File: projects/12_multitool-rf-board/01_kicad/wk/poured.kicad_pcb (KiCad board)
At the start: 4 copper layers, 150 x 150 mm, 87 parts, among them M1 vibro, SW1 RFswitch, SW2 RFswitch, U1 STM32WB55RG, U10 ESD, U2 CC1101, U3 ST25R3916, U5 ST7565R, U6 BQ25896, U7 BQ27220, U8 LM3281, U8B LM3281, U9 loadsw, X10 BAT+NTC, X6 FFC 18p, Y1 32MHz, Y2 32.768kHz

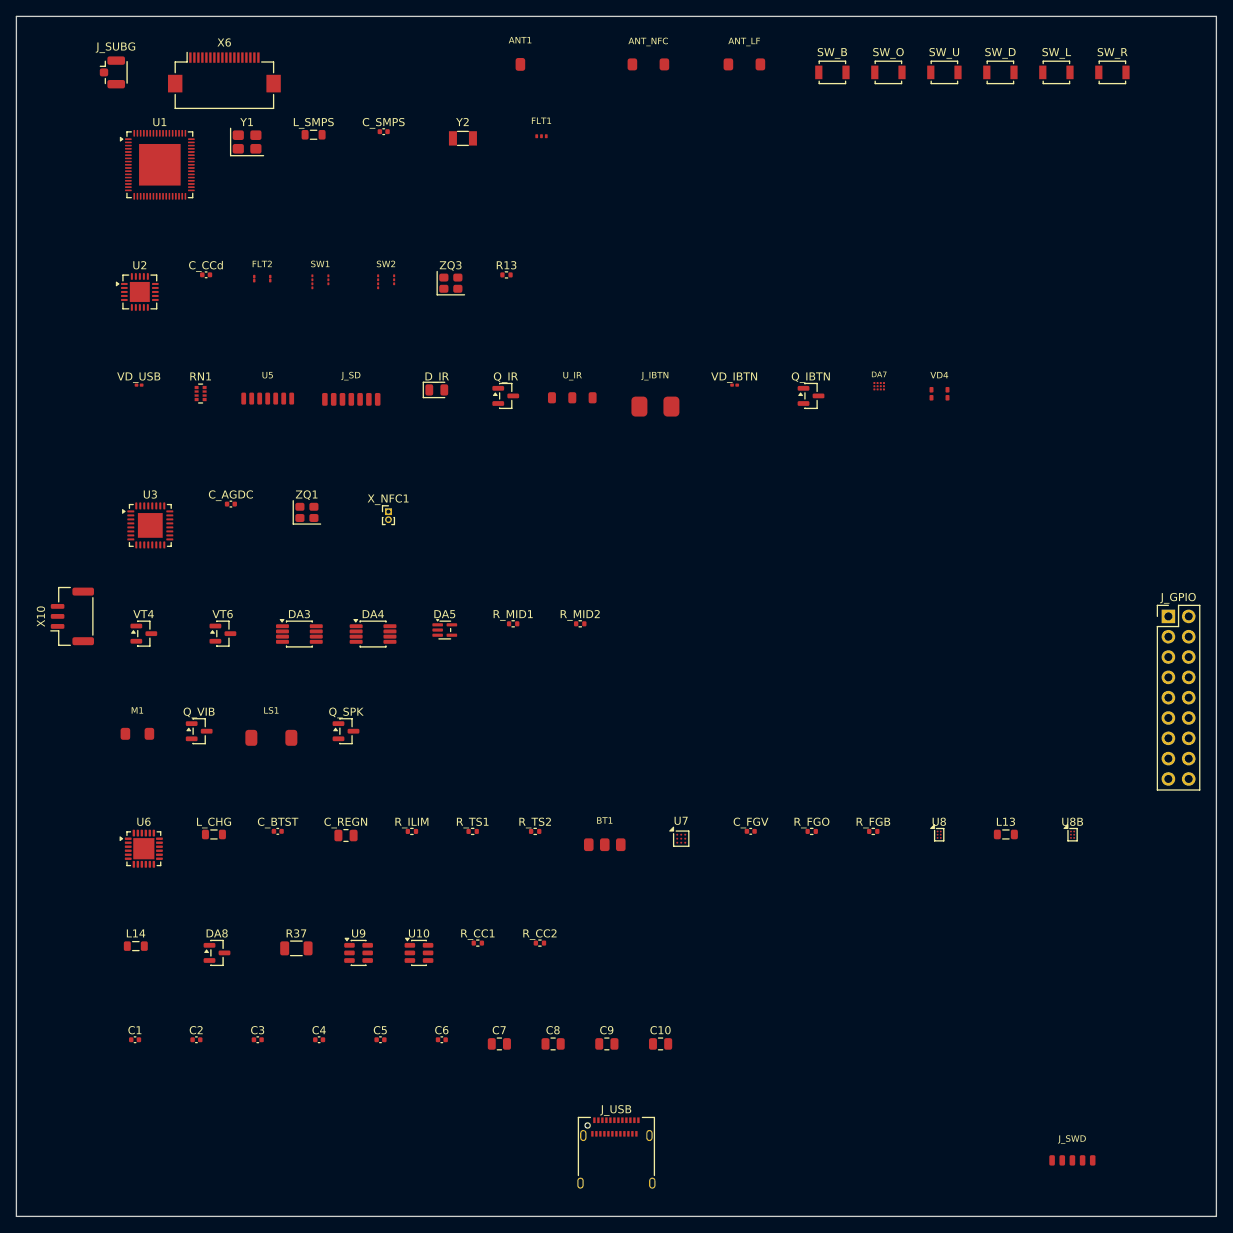
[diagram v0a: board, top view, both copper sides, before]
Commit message: proj12: compact two-sided board (110x66mm) - buildable
Reworked make_pcb.py for a compact, reference-proportion board:
- two-sided assembly: ICs/connectors/crystals on TOP, small passives + SOT-23
  FETs + SC-70 on BOTTOM (flipped), ~halving top-side area
- tighter GAP (1.2mm), largest-first row packing
- top interior inset clear of the left/right edge connectors (X10, J_GPIO);
  edge connectors/antennas/buttons respaced for the 110mm width
- board 110x66mm (was 150x150) ~ 1/3 the area; still original (own outline,
  no mascot/trademark)
check_assembly VERDICT: buildable (0 overlap, 0 pad-conflict, 0 off-board).
Routing the compact board in progress.

Co-Authored-By: Claude Opus 4.8 <noreply@anthropic.com>
Claude-Session: https://claude.ai/code/session_01Hk6s8R6up8HYVQWXd3atVk
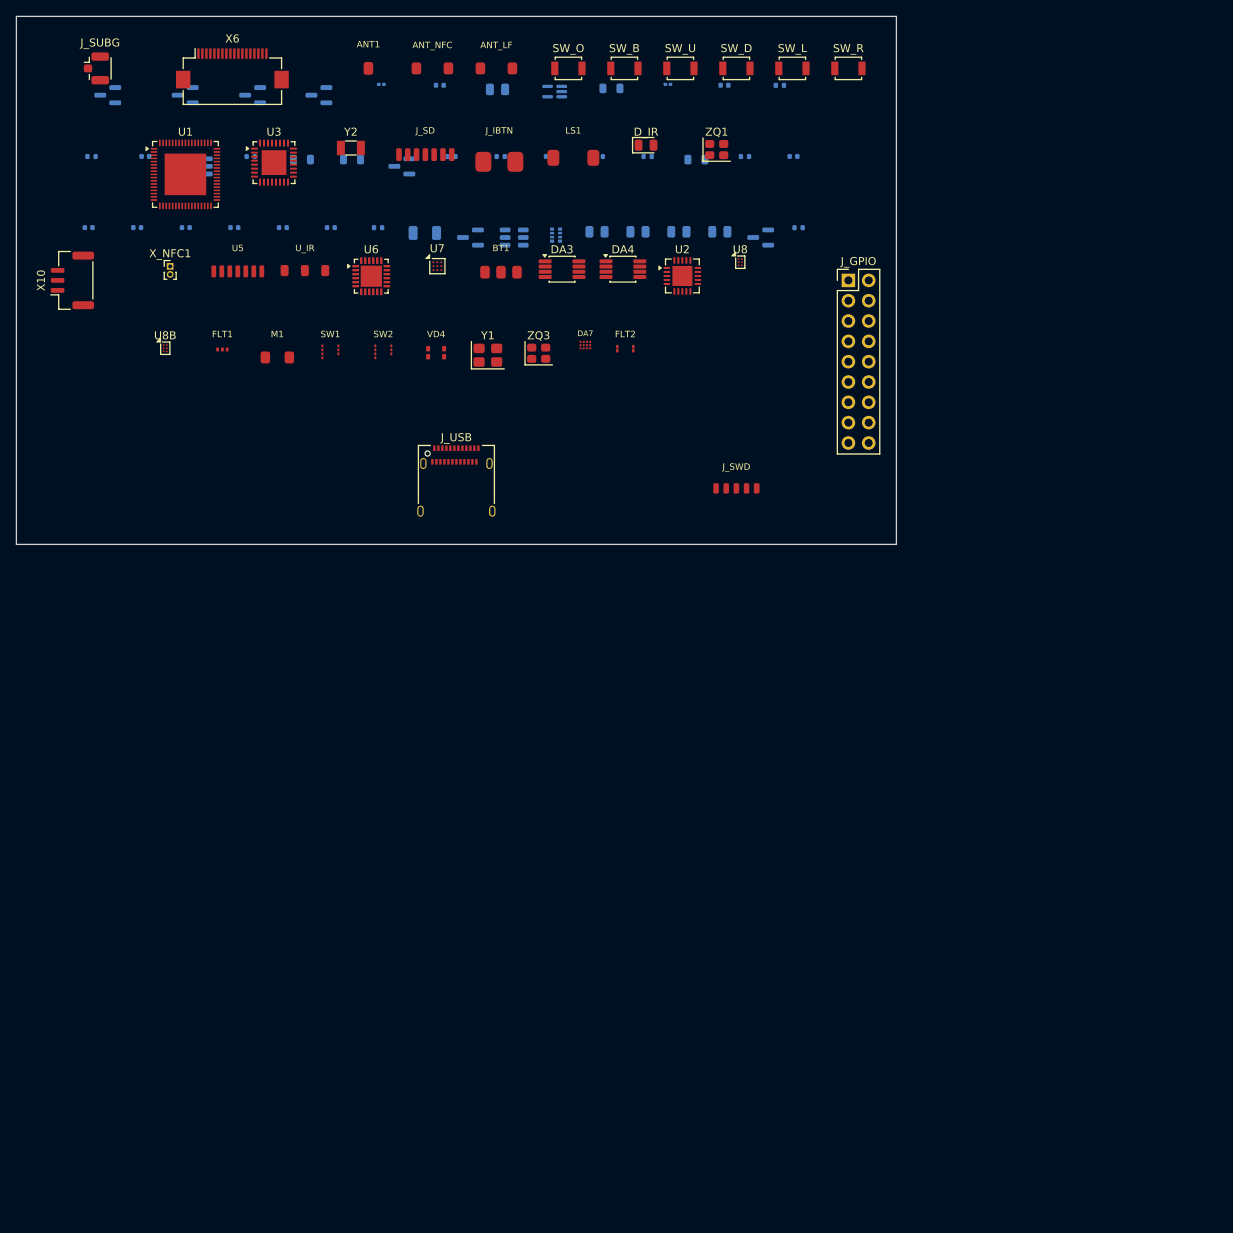
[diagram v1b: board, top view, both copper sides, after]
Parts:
- C1, C10, C2, C3, C4, C5, C6, C7, C8, C9, C_AGDC, C_BTST, C_CCd, C_FGV, C_REGN, C_SMPS, DA5, DA8, L13, L14, L_CHG, L_SMPS, Q_IBTN, Q_IR, Q_SPK, Q_VIB, R13, R37, RN1, R_CC1, R_CC2, R_FGB, R_FGO, R_ILIM, R_MID1, R_MID2, R_TS1, R_TS2, U10, U9, VD_IBTN, VD_USB, VT4, VT6: moved to B.Cu
- moved C1 137.7 mm to (127.1, 47.5), turned to 180 degrees
- moved U8B 128.7 mm to (48.6, 71.5)
- moved L13 121.9 mm to (65.7, 47.9), turned to 180 degrees
- moved DA8 108.1 mm to (41.4, 39.8), turned to 180 degrees
- moved L_CHG 103.7 mm to (115.0, 47.9), turned to 180 degrees
- moved C6 103.4 mm to (63.3, 56.4), turned to 180 degrees
- moved C5 103.2 mm to (57.2, 56.4), turned to 180 degrees
- moved C4 102.9 mm to (51.2, 56.4), turned to 180 degrees
- moved C3 102.6 mm to (45.1, 56.4), turned to 180 degrees
- moved C2 102.4 mm to (39.0, 56.4), turned to 180 degrees
- moved C7 102.3 mm to (102.6, 56.9), turned to 180 degrees
- moved C8 102.1 mm to (107.7, 56.9), turned to 180 degrees
- moved L14 102.0 mm to (72.0, 47.9), turned to 180 degrees
- moved C9 101.9 mm to (112.8, 56.9), turned to 180 degrees
- moved C10 101.8 mm to (117.9, 56.9), turned to 180 degrees
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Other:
- board size 150 x 150 mm -> 110 x 66 mm

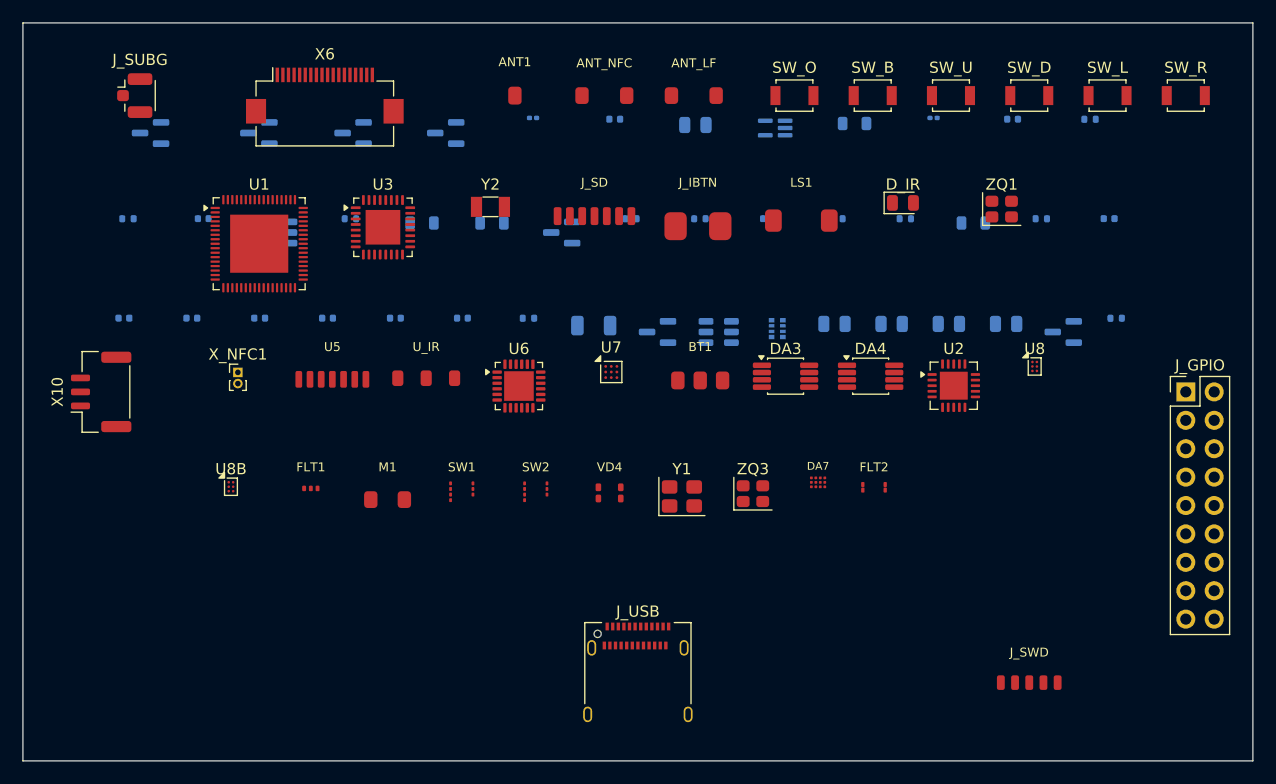
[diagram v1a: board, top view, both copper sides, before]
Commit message: proj12: smaller board 100x60mm, crystals clustered under their ICs
- crystal-cluster packing: Y1/Y2 under U1, ZQ3 under U2, ZQ1 under U3 (short
  OSC nets, signal integrity; fixes the LSE_OUT routing block)
- battery pack BT1 now off-board (external, wired via X10) - frees board area
- op-amps/DFN moved to bottom side, tighter GAP 0.7, INSET 5
- board 100x60mm (was 110x66) ~17% smaller; check_assembly: buildable
  (0 overlap, 0 off-board), 86 populated parts

Co-Authored-By: Claude Opus 4.8 <noreply@anthropic.com>
Claude-Session: https://claude.ai/code/session_01Hk6s8R6up8HYVQWXd3atVk
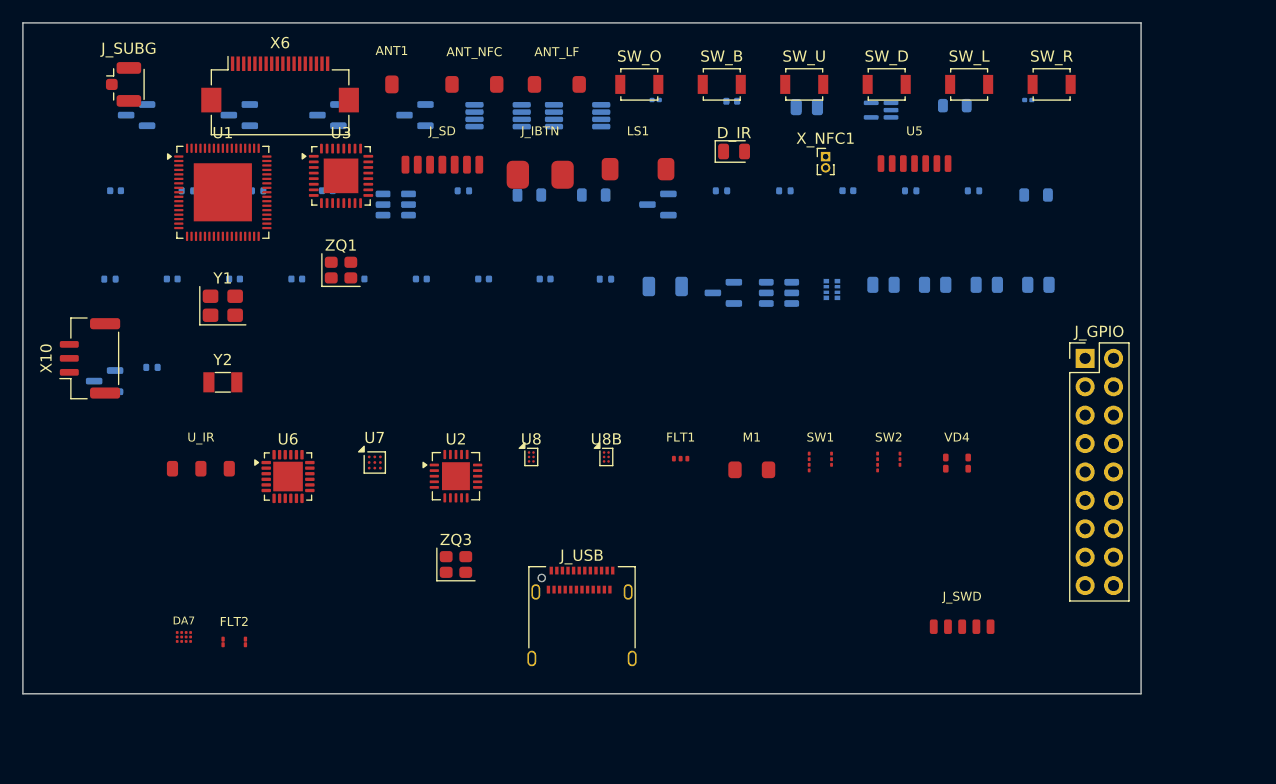
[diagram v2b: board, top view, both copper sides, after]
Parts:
- removed BT1: Li-Po 1S, crl-mt1:Battery_3p
- DA3, DA4: moved to B.Cu
- moved R13 86.3 mm to (41.5, 60.8)
- moved Q_IR 85.8 mm to (37.3, 62.0)
- moved C1 84.0 mm to (43.4, 52.9)
- moved R_FGB 83.5 mm to (37.8, 52.9)
- moved R_MID1 81.0 mm to (44.7, 45.0)
- moved C_AGDC 80.5 mm to (38.3, 45.0)
- moved ZQ1 59.3 mm to (58.4, 52.1)
- moved FLT2 58.9 mm to (48.9, 85.4)
- moved DA7 58.4 mm to (44.4, 84.9)
- moved X_NFC1 56.0 mm to (101.8, 42.0)
- moved U5 55.5 mm to (109.7, 42.6)
- moved U8 45.7 mm to (75.5, 68.8)
- moved U2 45.2 mm to (68.7, 70.5)
- moved Y1 44.5 mm to (47.9, 55.3)
- moved DA4 35.1 mm to (79.6, 38.3), turned to 180 degrees
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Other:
- board size 110 x 66 mm -> 100 x 60 mm

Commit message: proj12: NOVA-RF1 compact route 103/104 + both planes + full fab package
- +3V3 plane on In2.Cu (power nets closed), GND plane on In1.Cu
- 103/104 nets routed (NFC_CS needs 1 manual trace - only top+bottom free on a
  2-plane 4-layer board), 2965 segments, 530 vias; silkscreen added
- fab package: Gerber X2 + Excellon drill + map, CPL, JLCPCB + costed BOM
  (03_fab/NOVA-RF1_gerbers.zip etc.), names corrected in fab_export.sh
- refreshed routed-board render + product PDF; PCB_STATUS.md final section

Co-Authored-By: Claude Opus 4.8 <noreply@anthropic.com>
Claude-Session: https://claude.ai/code/session_01Hk6s8R6up8HYVQWXd3atVk
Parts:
- ANT1: footprint crl-mt1:Antenna_Chip -> nova-rf1:Antenna_Chip
- ANT_LF: footprint crl-mt1:RFID_125k_Coil -> nova-rf1:RFID_125k_Coil
- ANT_NFC: footprint crl-mt1:NFC_Loop_Antenna -> nova-rf1:NFC_Loop_Antenna
- DA7: footprint crl-mt1:LP5562_DSBGA12 -> nova-rf1:LP5562_DSBGA12
- FLT1: footprint crl-mt1:RF_filter -> nova-rf1:RF_filter
- FLT2: footprint crl-mt1:Johanson_0310_Balun -> nova-rf1:Johanson_0310_Balun
- J_IBTN: footprint crl-mt1:iButton_Contacts -> nova-rf1:iButton_Contacts
- J_SD: footprint crl-mt1:microSD_7p -> nova-rf1:microSD_7p
- J_SWD: footprint crl-mt1:TagConnect_TC2030 -> nova-rf1:TagConnect_TC2030
- LS1: footprint crl-mt1:Speaker_2p -> nova-rf1:Speaker_2p
- M1: footprint crl-mt1:Vibro_2p -> nova-rf1:Vibro_2p
- SW1, SW2: footprint crl-mt1:RF_Switch_TSNP9 -> nova-rf1:RF_Switch_TSNP9
- U5: footprint crl-mt1:Display_ST7565_FFC -> nova-rf1:Display_ST7565_FFC
- U_IR: footprint crl-mt1:TSOP_IR_3p -> nova-rf1:TSOP_IR_3p
- VD4: footprint crl-mt1:LED_RGB_4p -> nova-rf1:LED_RGB_4p
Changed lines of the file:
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@@
 	(net 176 "unconnected-(U9-4)")
 	(net 177 "unconnected-(U9-5)")
-	(footprint "crl-mt1:Display_ST7565_FFC"
+	(footprint "nova-rf1:Display_ST7565_FFC"
 		(layer "F.Cu")
 		(at 109.739287 42.5786)
@@
 		(embedded_fonts no)
 	)
-	(footprint "crl-mt1:iButton_Contacts"
+	(footprint "nova-rf1:iButton_Contacts"
 		(layer "F.Cu")
 		(at 76.263095 43.5786)
@@
 		)
 	)
-	(footprint "crl-mt1:Speaker_2p"
+	(footprint "nova-rf1:Speaker_2p"
 		(layer "F.Cu")
 		(at 85.013095 43.0786)
@@
 		)
 	)
-	(footprint "crl-mt1:microSD_7p"
+	(footprint "nova-rf1:microSD_7p"
 		(layer "F.Cu")
 		(at 67.513095 42.6786)
@@
 		(embedded_fonts no)
 	)
-	(footprint "crl-mt1:RF_Switch_TSNP9"
+	(footprint "nova-rf1:RF_Switch_TSNP9"
 		(layer "F.Cu")
 		(at 101.318096 69.2681)
@@
 		)
 	)
-	(footprint "crl-mt1:RFID_125k_Coil"
+	(footprint "nova-rf1:RFID_125k_Coil"
 		(locked yes)
 		(layer "F.Cu")
@@
 		(embedded_fonts no)
 	)
-	(footprint "crl-mt1:LP5562_DSBGA12"
+	(footprint "nova-rf1:LP5562_DSBGA12"
 		(layer "F.Cu")
 		(at 44.396667 84.917499)
@@
 		)
 	)
-	(footprint "crl-mt1:NFC_Loop_Antenna"
+	(footprint "nova-rf1:NFC_Loop_Antenna"
 		(locked yes)
 		(layer "F.Cu")
@@
 		(embedded_fonts no)
 	)
-	(footprint "crl-mt1:Johanson_0310_Balun"
+	(footprint "nova-rf1:Johanson_0310_Balun"
 		(layer "F.Cu")
 		(at 48.900479 85.3611)
@@
 		)
 	)
-	(footprint "crl-mt1:TSOP_IR_3p"
+	(footprint "nova-rf1:TSOP_IR_3p"
 		(layer "F.Cu")
 		(at 45.915 69.8681)
@@
 		)
 	)
-	(footprint "crl-mt1:LED_RGB_4p"
+	(footprint "nova-rf1:LED_RGB_4p"
 		(layer "F.Cu")
 		(at 113.537143 69.3681)
@@
 		)
 	)
-	(footprint "crl-mt1:Antenna_Chip"
+	(footprint "nova-rf1:Antenna_Chip"
 		(locked yes)
 		(layer "F.Cu")
@@
 		(embedded_fonts no)
 	)
-	(footprint "crl-mt1:RF_filter"
+	(footprint "nova-rf1:RF_filter"
 		(layer "F.Cu")
 		(at 88.820477 68.9681)
@@
 		(embedded_fonts no)
 	)
-	(footprint "crl-mt1:RF_Switch_TSNP9"
+	(footprint "nova-rf1:RF_Switch_TSNP9"
 		(layer "F.Cu")
 		(at 107.437143 69.2681)
@@
 		)
 	)
-	(footprint "crl-mt1:Vibro_2p"
+	(footprint "nova-rf1:Vibro_2p"
 		(layer "F.Cu")
 		(at 95.183573 69.9681)
@@
 		(embedded_fonts no)
 	)
-	(footprint "crl-mt1:TagConnect_TC2030"
+	(footprint "nova-rf1:TagConnect_TC2030"
 		(locked yes)
 		(layer "F.Cu")
